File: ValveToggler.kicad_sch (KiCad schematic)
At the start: 72 parts, among them J1 24V IN, J17 MODE (24V), J2 Coil2, J3 Coil1, Q1 IRFZ24N, Q10 2N7000, Q11 2N7000, Q2 2N7000, Q3 IRFZ24N, Q4 2N7000, Q6 BC557, Q7 2N7000, Q8 BC557, Q9 2N7000, U2 NE555P, U3 L7812, U4 NE555P, U9 LM2576T-5

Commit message: Rework logic (drop PNP, default on coil, pulldown-OR)
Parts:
- removed Q6, Q8: BC557, Package_TO_SOT_THT:TO-92_Inline, symbol Transistor_BJT:BC557
- removed R14, R18: 47k, Resistor_THT:R_Axial_DIN0207_L6.3mm_D2.5mm_P10.16mm_Horizontal, symbol Device:R
- removed R19, R20: 100k, Resistor_THT:R_Axial_DIN0207_L6.3mm_D2.5mm_P10.16mm_Horizontal, symbol Device:R
- removed R7: 2k2, Resistor_THT:R_Axial_DIN0207_L6.3mm_D2.5mm_P10.16mm_Horizontal, symbol Device:R
- added Q5, Q6: 2N7000, Package_TO_SOT_THT:TO-92_HandSolder, symbol Transistor_FET:2N7000
- C4: value 10u -> 47u
- R11: now not fitted; now left out of the parts list
- R12, R4: value 2k2 -> 1k5
- R22: value 100 -> 330
- R24, R8: value 2k2 -> 10k
- R6: value 100k -> 10k
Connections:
- net GNDPWR is gone; now on net GND: C10.2, C19.2, C20.2, D1.2 (A), D5.2 (A), J1.2 (Pin_2), OC21.3, Q1.3 (S), Q2.1 (S), Q3.3 (S), R11.2, R6.2, U3.2 (GND)
- net +12V: now also R8.1, R9.2
- net GND: now also Q5.1 (S), Q6.1 (S); no longer R8.2
- net MODE_DOUBLE_12V: no longer U2.4 (R)
- net MOS2: now also Q7.3 (D), R22.1, R9.1, Q6.3 (D); no longer Q3.1 (G), R11.1, R22.2
- net NOT_MODE_DOUBLE: now also Q5.2 (G), Q6.2 (G)
- net at Q10.3 (D), Q4.3 (D), R24.2: now also U4.4 (R)
- new net: Q3.1 (G), R11.1, R22.2
- new net: Q5.3 (D), R8.2, U2.4 (R)
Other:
- note added: "always force coil2 off when not in DOUBLE-MODE"
- note added: "invert mode2 signal -> Coil2 runs complementary to Coil1"
- note added: "reset condition for mode2-DOUBLE"
- note removed: "default off"
- note removed: "force coil2 off when not in DOUBLE-MODE"
- note removed: "invert mode2 signal (coils run complementary)"
- moved on the sheet: C1, C2, C3, C4, D10, D11, D2, D3, D6, D7, D8, D9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

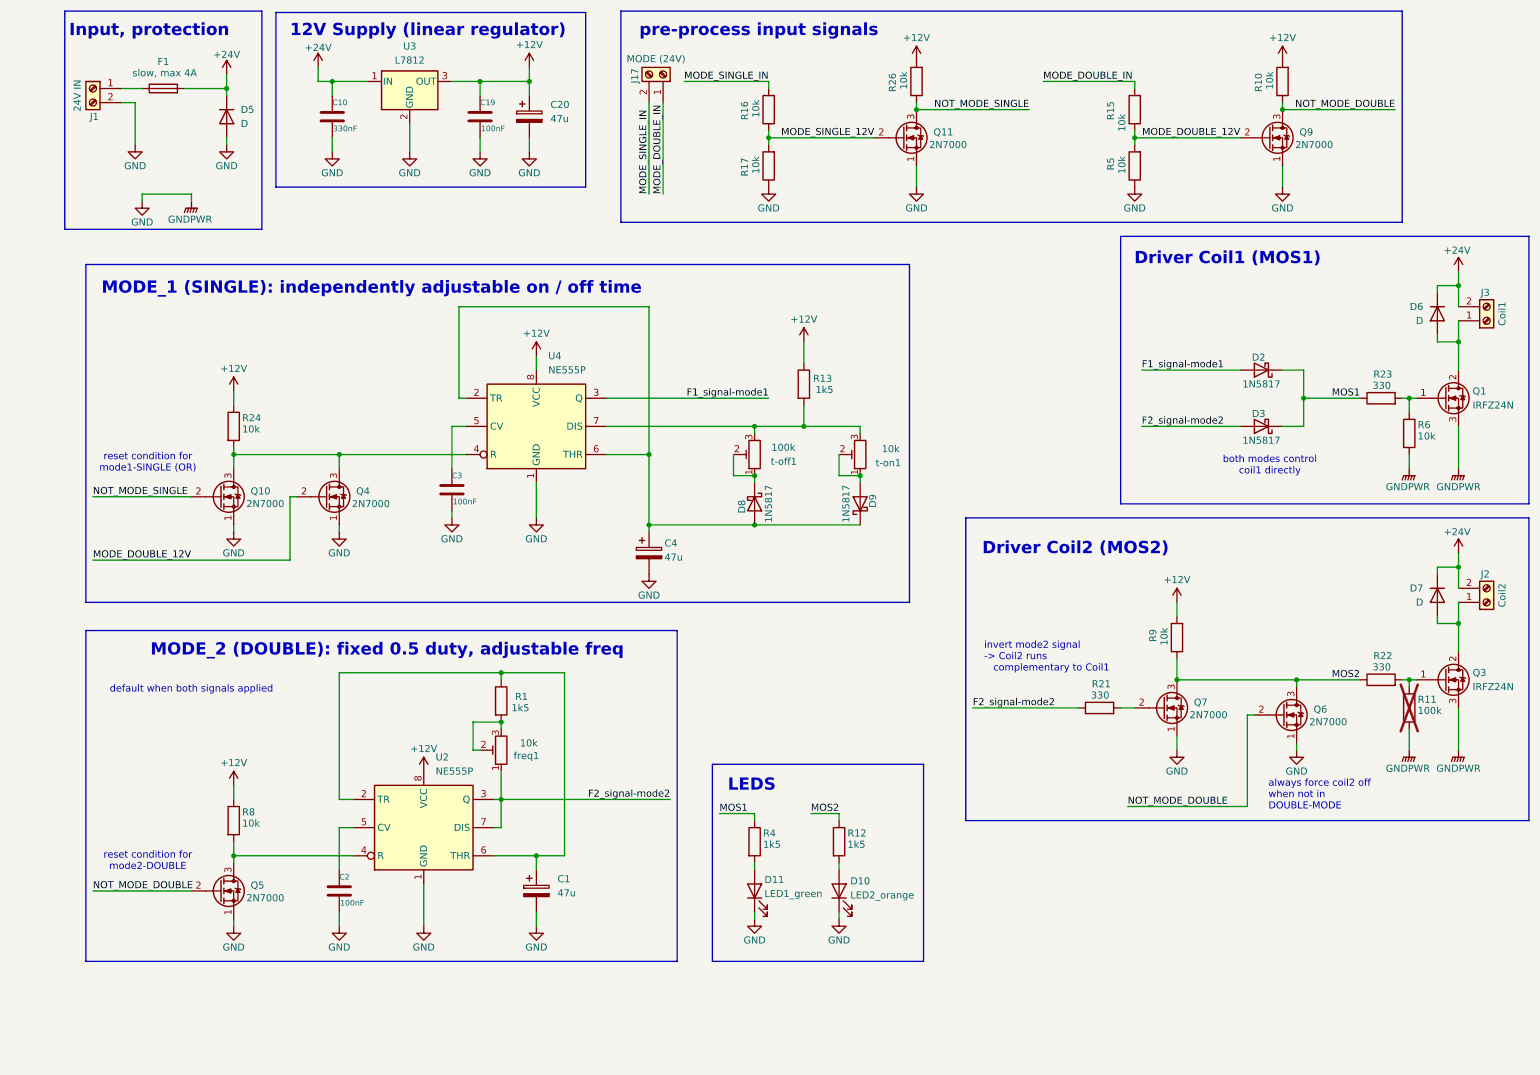
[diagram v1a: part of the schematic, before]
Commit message: Optimize logic (more current, but significantly fewer parts)
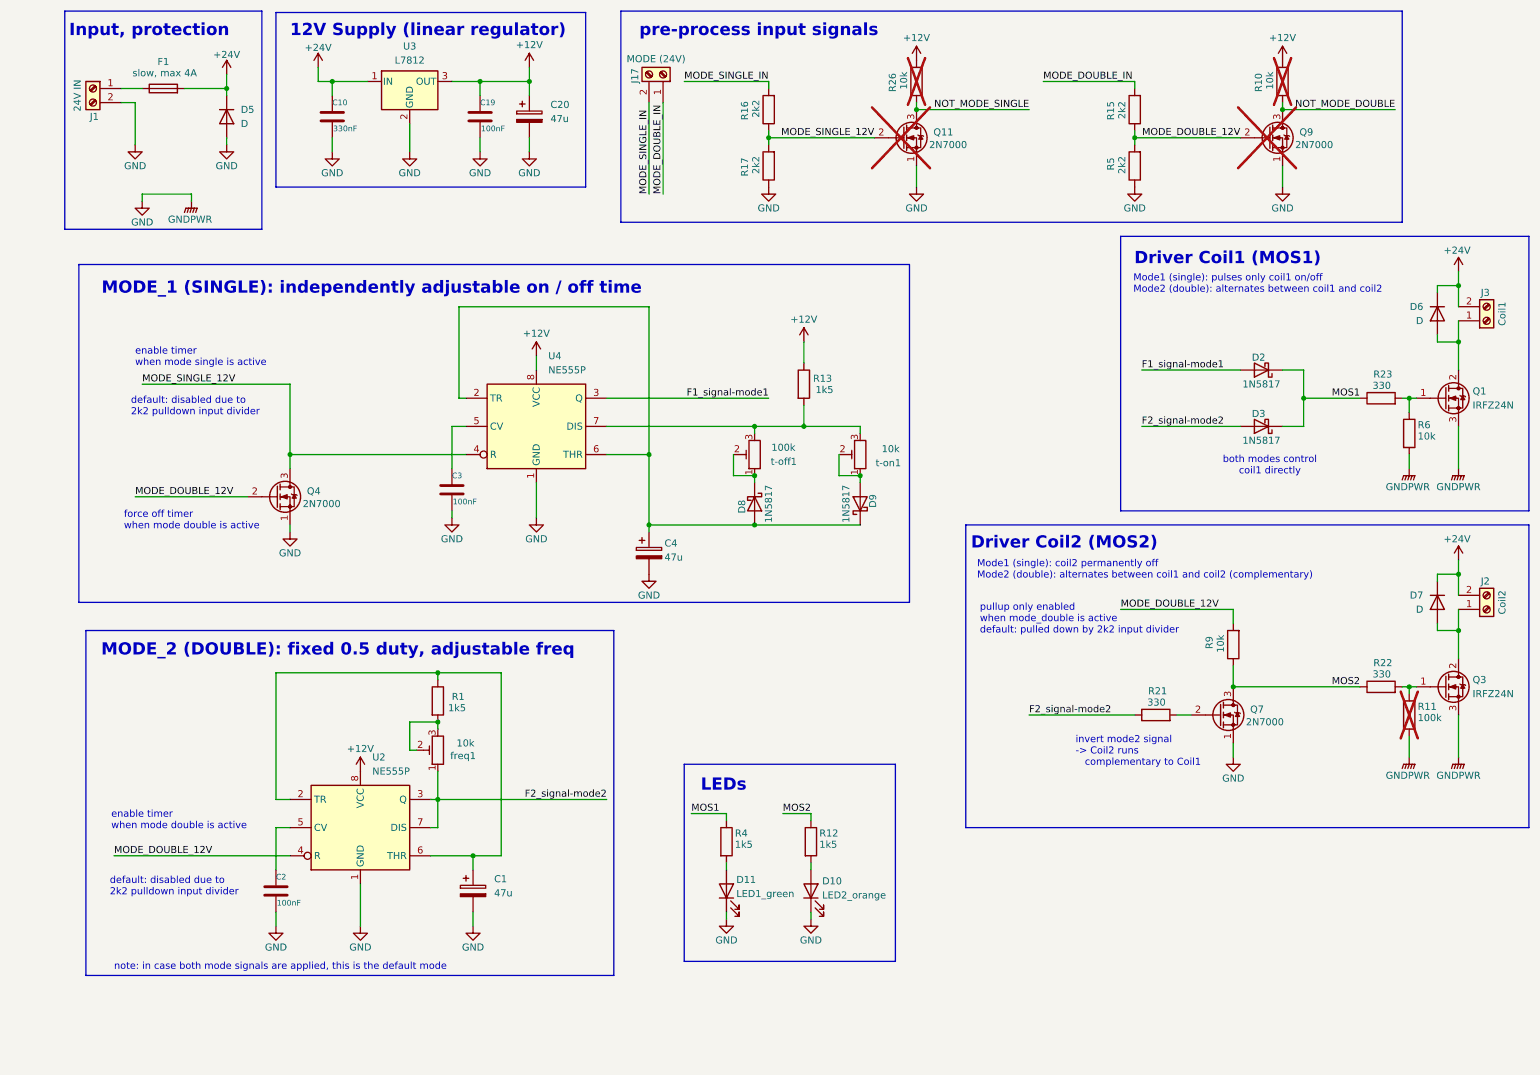
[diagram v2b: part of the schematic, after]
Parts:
- removed Q10, Q5, Q6: 2N7000, Package_TO_SOT_THT:TO-92_HandSolder, symbol Transistor_FET:2N7000
- removed R24, R8: 10k, Resistor_THT:R_Axial_DIN0207_L6.3mm_D2.5mm_P10.16mm_Horizontal, symbol Device:R
- D5, D6, D7: footprint Diode_THT:D_T-1_P12.70mm_Horizontal -> Diode_THT:D_DO-41_SOD81_P5.08mm_Vertical_AnodeUp
- Q11, Q9, R10, R26: now not fitted; now left out of the parts list
- R13: footprint Resistor_THT:R_Axial_DIN0207_L6.3mm_D2.5mm_P10.16mm_Horizontal -> Resistor_THT:R_Axial_DIN0207_L6.3mm_D2.5mm_P2.54mm_Vertical
- R15, R16, R17, R5: value 10k -> 2k2
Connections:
- net +12V: no longer R9.2
- net MODE_DOUBLE_12V: now also R9.2, U2.4 (R)
- net MODE_SINGLE_12V: now also Q4.3 (D), U4.4 (R)
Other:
- note added: "LEDs"
- note added: "Mode1 (single): coil2 permanently off Mode2 (double): alternates between coil1 and coil2 (complementary)"
- note added: "Mode1 (single): pulses only coil1 on/off Mode2 (double): alternates between coil1 and coil2"
- note added: "default: disabled due to 2k2 pulldown input divider"
- note added: "enable timer when mode double is active"
- note added: "enable timer when mode single is active"
- note added: "force off timer when mode double is active"
- note added: "note: in case both mode signals are applied, this is the default mode"
- note added: "pullup only enabled when mode_double is active default: pulled down by 2k2 input divider"
- note removed: "LEDS"
- note removed: "always force coil2 off when not in DOUBLE-MODE"
- note removed: "default when both signals applied"
- note removed: "reset condition for mode1-SINGLE (OR)"
- note removed: "reset condition for mode2-DOUBLE"
- moved on the sheet: C1, C2, D10, D11, D7, J2, Q3, Q4, Q7, R1, R11, R12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

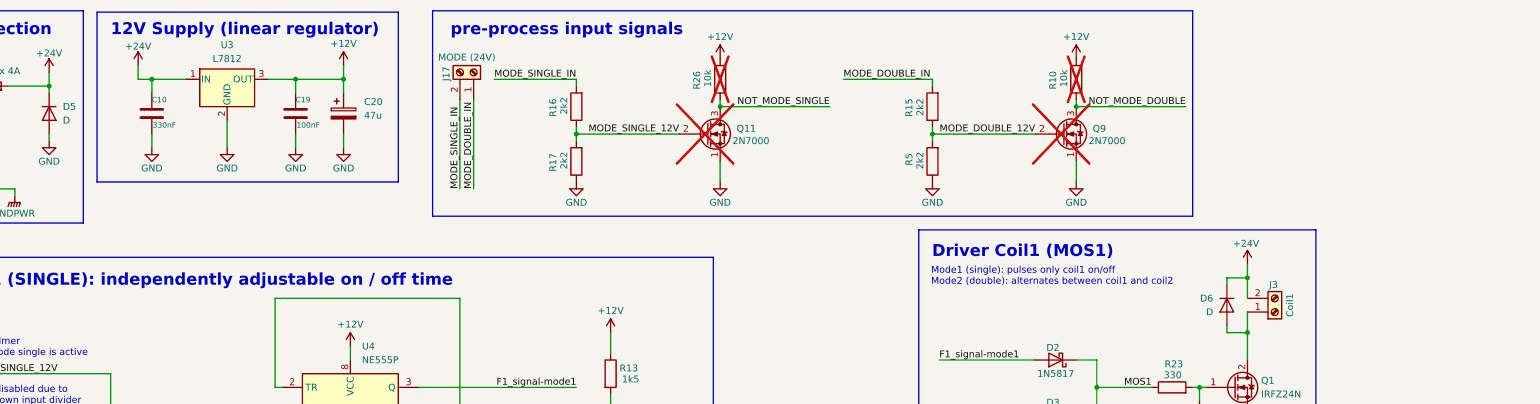
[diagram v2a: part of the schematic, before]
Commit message: Routing complete, DRC pass
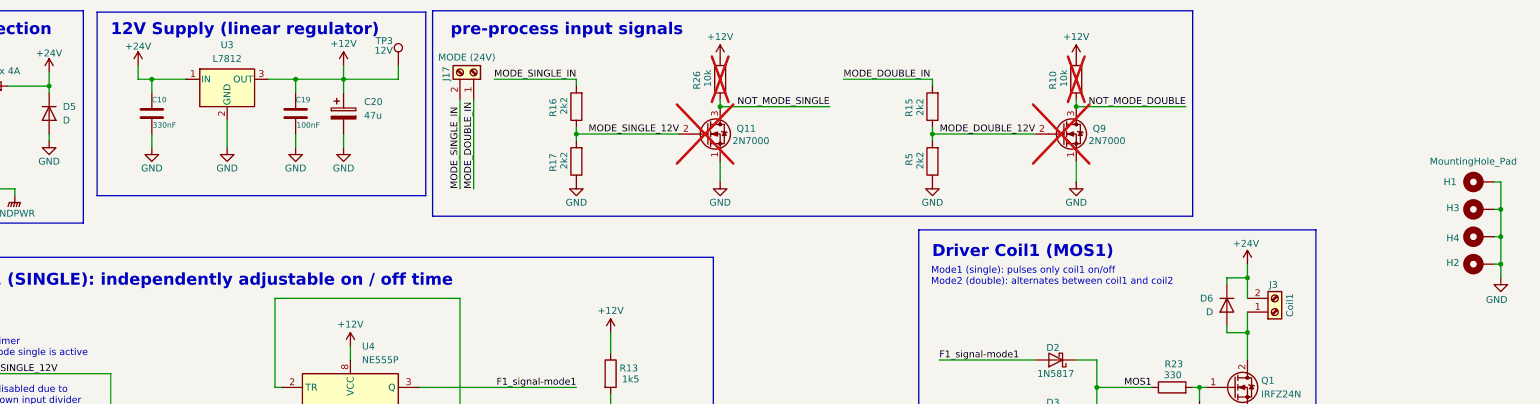
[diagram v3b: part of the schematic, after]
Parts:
- added H1, H2, H3, H4: MountingHole_Pad, mountingHoles_libJonny:MountingHole_2.2mm_NPTH-with-pad_DRC-clearance-error, symbol Mechanical:MountingHole_Pad
- added TP3: 12V, Connector_PinHeader_2.54mm:PinHeader_1x01_P2.54mm_Vertical, symbol Connector:TestPoint
- R1: footprint Resistor_THT:R_Axial_DIN0207_L6.3mm_D2.5mm_P2.54mm_Vertical -> Resistor_THT:R_Axial_DIN0207_L6.3mm_D2.5mm_P10.16mm_Horizontal
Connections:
- net +12V: now also TP3.1
- net GND: now also H1.1, H2.1, H3.1, H4.1

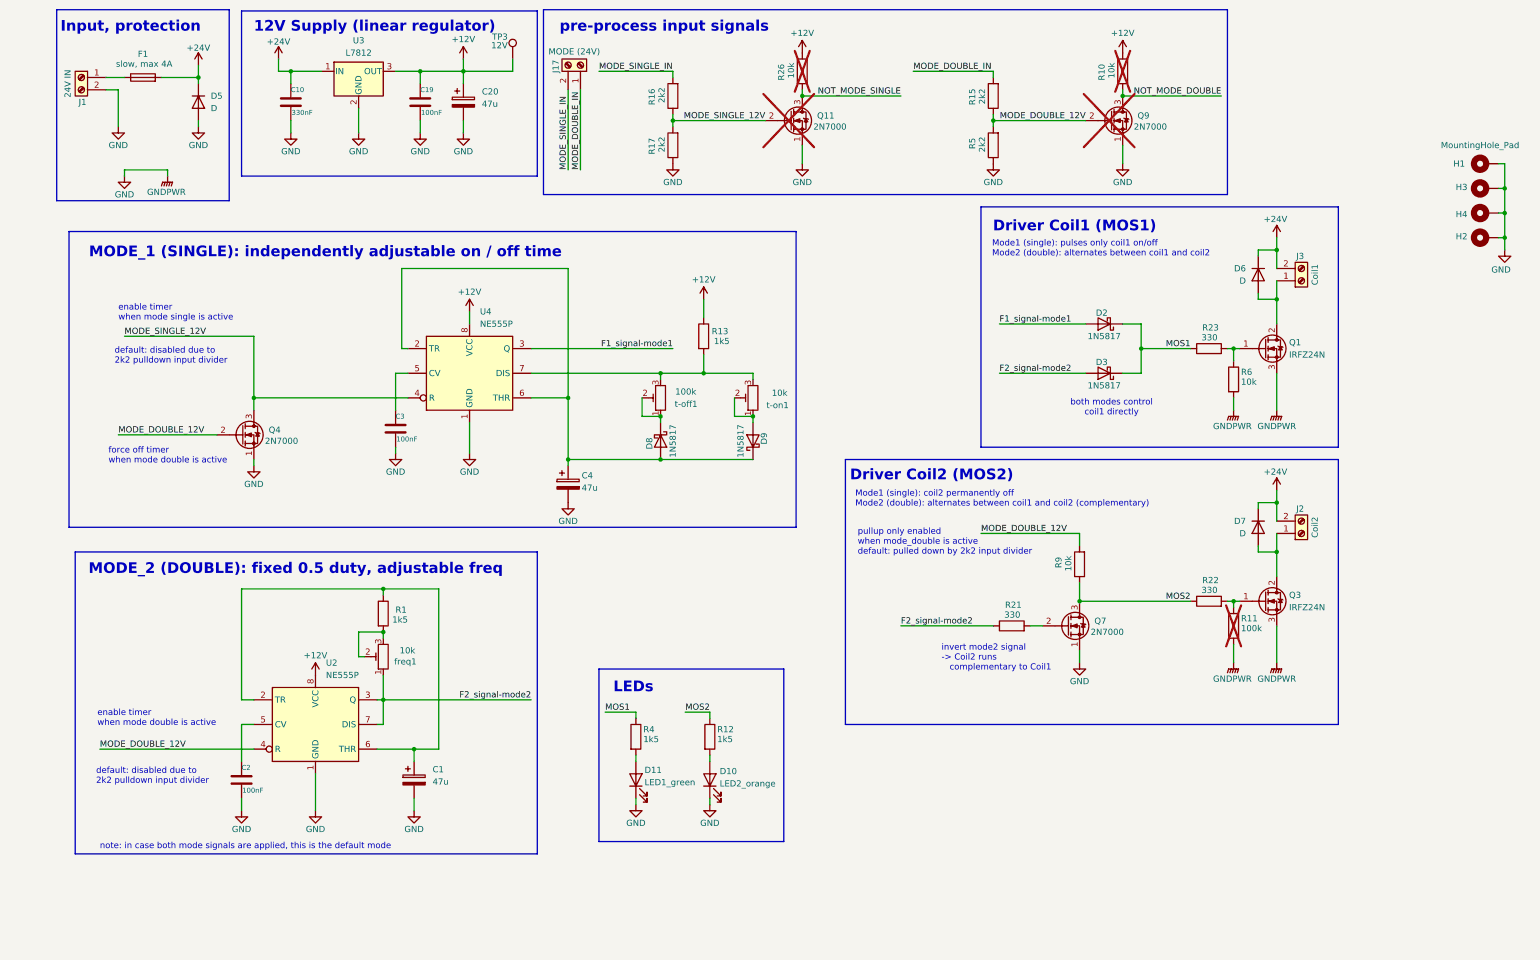
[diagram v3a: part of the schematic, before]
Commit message: Add R to trimmer (offMin), rework routing, Add timing calculation notes
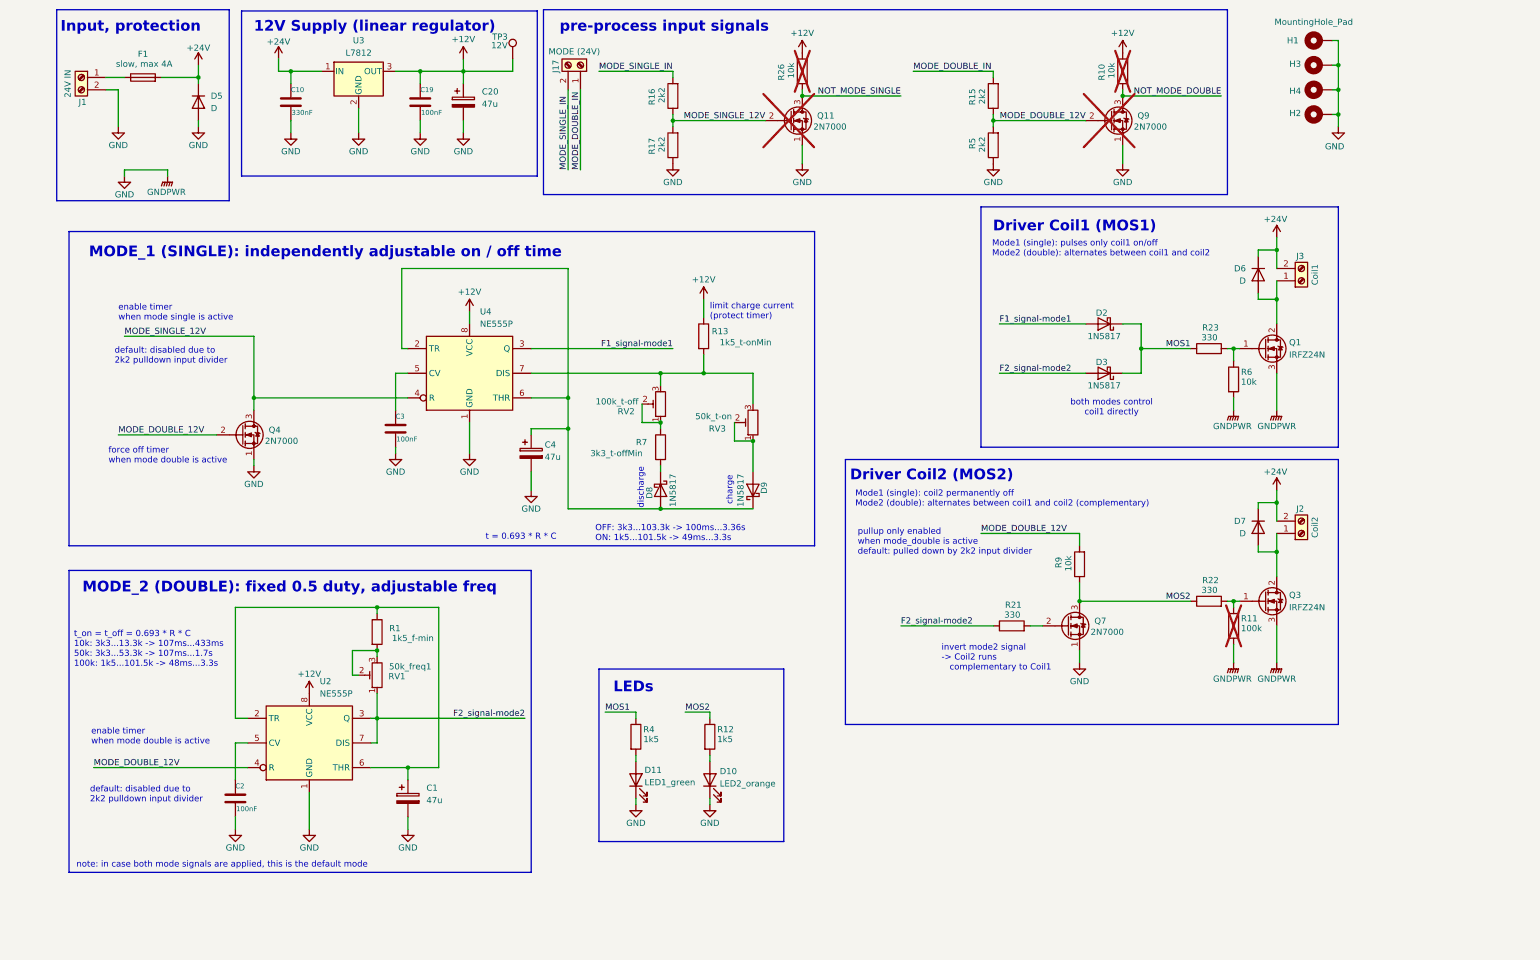
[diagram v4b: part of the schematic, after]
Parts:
- added R7: 3k3_t-offMin, Resistor_THT:R_Axial_DIN0207_L6.3mm_D2.5mm_P10.16mm_Horizontal, symbol Device:R
- R1: value 1k5 -> 1k5_f-min
- R13: value 1k5 -> 1k5_t-onMin
- RV1: renamed from freq1; value 10k -> 50k_freq1; footprint Potentiometer_THT:Potentiometer_Piher_PT-10-V10_Vertical -> resistors_libJonny:Potentiometer_Piher_PT-10-V10_Vertical
- RV2: renamed from t-off1; value 100k -> 100k_t-off; footprint Potentiometer_THT:Potentiometer_Piher_PT-10-V10_Vertical -> resistors_libJonny:Potentiometer_Piher_PT-10-V10_Vertical
- RV3: renamed from t-on1; value 10k -> 50k_t-on; footprint Potentiometer_THT:Potentiometer_Piher_PT-10-V10_Vertical -> resistors_libJonny:Potentiometer_Piher_PT-10-V10_Vertical
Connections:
- net at RV2.1, RV2.2: now also R7.1; no longer D8.1 (K)
- new net: D8.1 (K), R7.2
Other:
- note added: "OFF: 3k3...103.3k -> 100ms...3.36s ON: 1k5...101.5k -> 49ms...3.3s"
- note added: "charge"
- note added: "discharge"
- note added: "limit charge current (protect timer)"
- note added: "t = 0.693 * R * C"
- note added: "t_on = t_off = 0.693 * R * C 10k: 3k3...13.3k -> 107ms...433ms 50k: 3k3...53.3k -> 107ms...1.7s 100k: 1k5...101.5k -> 48ms...3.3s"
- moved on the sheet: C1, C2, C4, D8, D9, H1, H2, H3, H4, R1, RV1, RV2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
